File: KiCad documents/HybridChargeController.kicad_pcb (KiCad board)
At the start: 2 copper layers, 87 x 87 mm, 101 parts, among them P1 Load, P2 LI_balancer, P3 PV, P4 Extra, P5 LI, P6 LA, Q1 MMBT3904, Q10 MMBT3904, Q11 IPD90P04P4L-04, Q12 STL60P4LLF6, Q13 STL60P4LLF6, Q14 IPD90P04P4L-04, Q15 BSS138, Q16 BSS138, Q2 IPD90P04P4L-04, Q3 MMBT3904, Q4 IPD90P04P4L-04, Q5 IPD90P04P4L-04, Q6 MMBT3904, Q7 MMBT3904, Q8 MMBT3904, Q9 IPD90P04P4L-04, U1 LM358D, U2 bq76920, U3 cd4051, U4 LM358D, U5 LM358D

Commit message: ready for review
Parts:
- added G***: LOGO, MEI_logo:soldesign-logo, F.Cu at (164.9, 109.2)
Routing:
- net /GND: track 17.1 -> 60.8 mm, vias 4 -> 24
- net /COM+: track 178.3 -> 184.6 mm
- net /LOAD+: track 7.32 -> 13.6 mm
- net /LI+: track 32.7 -> 39.0 mm
- net Net-(F1-Pad2): track 20.0 -> 24.9 mm
- net Net-(R20-Pad1): track 6.08 -> 10.6 mm, vias 2 -> 0
- net Net-(F2-Pad2): track 22.1 -> 25.9 mm
- net /SDA3: track 11.9 -> 13.9 mm
- net Net-(R11-Pad1): track 8.50 -> 9.20 mm
- added copper zone on F.Cu, net /COM+
- added copper zone on B.Cu, net /GND
- added copper zone on F.Cu, net /GND
- added copper zone on F.Cu, net /LA+
- added copper zone on F.Cu, net /LA-
- added copper zone on F.Cu, net /LI-
- added copper zone on F.Cu, net /LOAD+
- added copper zone on F.Cu, net /LOAD-
- added copper zone on F.Cu, net /PV+
- added copper zone on F.Cu, net /PV-
- added copper zone on F.Cu, net Net-(D3-Pad2)
- added copper zone on F.Cu, net Net-(F1-Pad1)
- added copper zone on F.Cu, net Net-(F1-Pad2)
- added copper zone on F.Cu, net Net-(F2-Pad1)
- added copper zone on F.Cu, net Net-(F2-Pad2)
- added copper zone on F.Cu, net Net-(Q14-Pad3)
- added copper zone on F.Cu, net Net-(Q4-Pad3)
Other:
- board text added: "3.3V"
- board text added: "5V"
- board text added: "Alrt"
- board text added: "COM+"
- board text added: "Cell 1-2"
- board text added: "Cell 2-3"
- board text added: "Cell 3-4"
- board text added: "GND"
- board text added: "Hybrid Charge Controller"
- board text added: "LED"
- board text added: "MA"
- board text added: "MB"
- board text added: "MC"
- board text added: "MISO"
- board text added: "MO"
- board text added: "MOSI"
- board text added: "RST"
- board text added: "RX"
- board text added: "SCK"
- board text added: "SCL"
- board text added: "SDA"
- board text added: "SW LA"
- board text added: "SW LD"
- board text added: "SW PV"
- board text added: "TX"
- board text added: "made for Karana by"

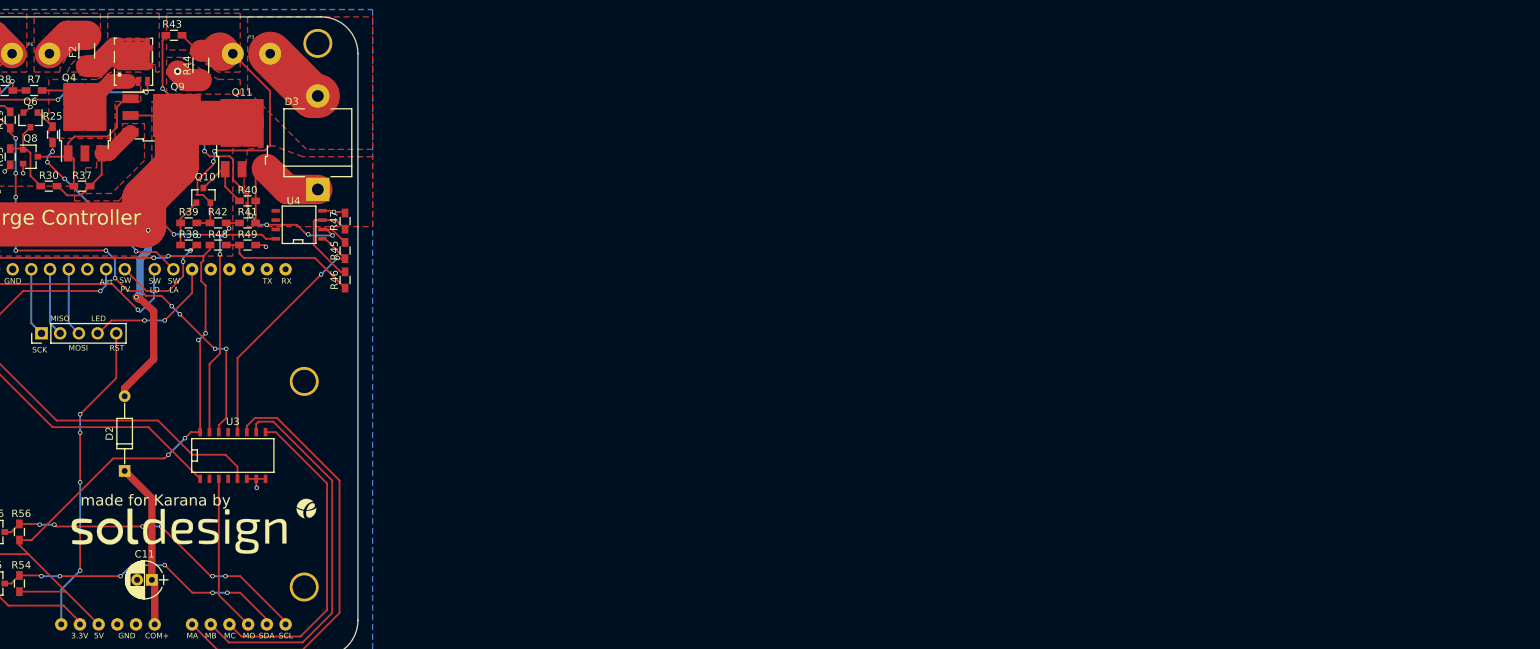
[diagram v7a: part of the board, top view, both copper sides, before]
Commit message: added a few comments for final check, played with the Silkscreen a bit
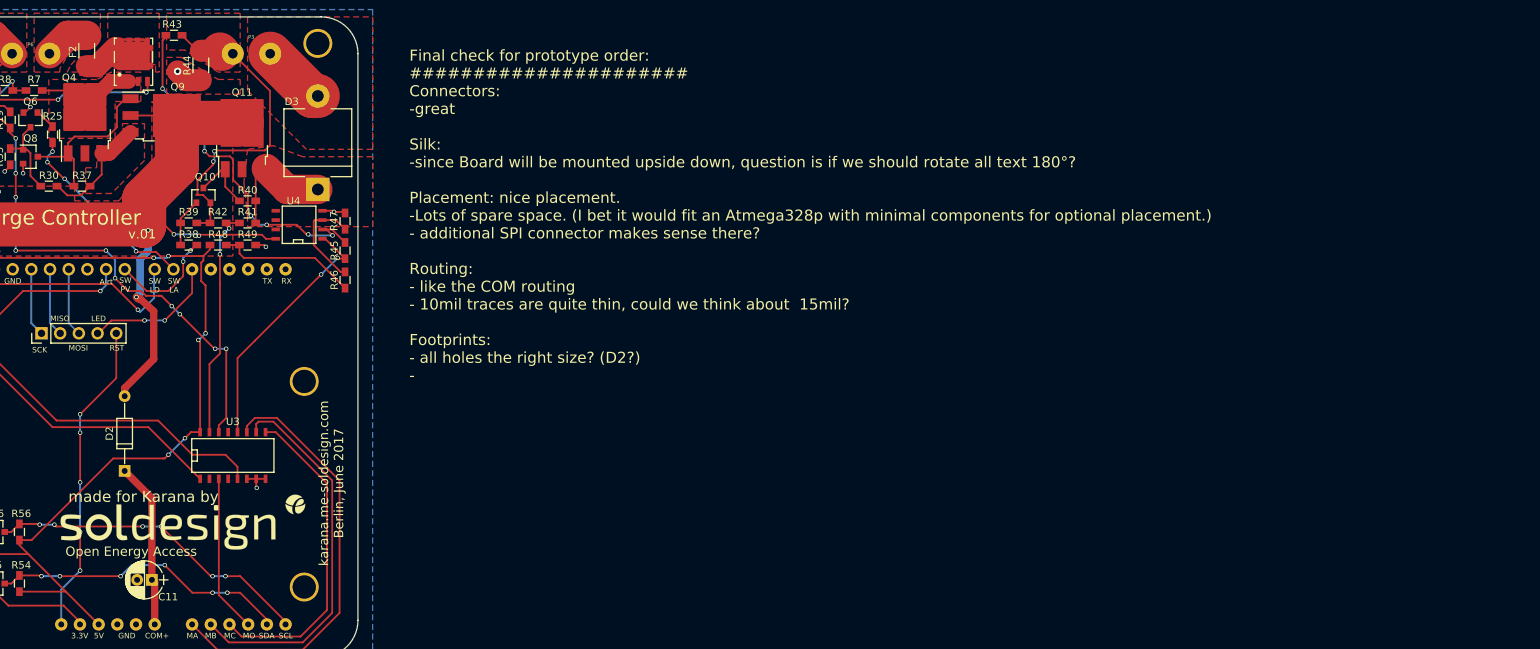
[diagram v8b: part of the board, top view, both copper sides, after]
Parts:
- moved G*** 1.60 mm to (163.4, 108.6)
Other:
- board text added: "Final check for prototype order: ###################### Connectors: -great Silk: -since Board will be mounted upside down, question is if we should rotate all text 180°? Placement: nice placement. -Lots of spare space. (I bet it would fit an Atmega328p with minimal components for optional placement.) - additional SPI connector makes sense there? Routing: - like the COM routing - 10mil traces are 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"
- board text added: "Open Energy Access"
- board text added: "karana.me-soldesign.com Berlin, June 2017"
- board text added: "v.01"
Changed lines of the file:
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@@
-(kicad_pcb (version 4) (host pcbnew 4.0.4-stable)
+(kicad_pcb (version 4) (host pcbnew 4.0.4+e1-6308~48~ubuntu15.10.1-stable)
   (general
     (links 248)
     (no_connects 2)
-    (area 99.924999 39.924999 187.075001 127.075001)
+    (area 97 39 189.000001 129.000001)
     (thickness 1.6)
-    (drawings 37)
+    (drawings 41)
     (tracks 866)
     (zones 0)
@@
     (0 F.Cu signal)
     (31 B.Cu signal hide)
-    (32 B.Adhes user)
-    (33 F.Adhes user)
+    (32 B.Adhes user hide)
+    (33 F.Adhes user hide)
     (34 B.Paste user)
     (35 F.Paste user)
@@
     (descr "CP, Radial series, Radial, pin pitch=2.00mm, , diameter=5mm, Electrolytic Capacitor")
     (tags "CP Radial series Radial pin pitch 2.00mm  diameter 5mm Electrolytic Capacitor")
-    (fp_text reference C11 (at 1 3.5 180) (layer F.SilkS)
+    (fp_text reference C11 (at -2.2138 -2.3212 180) (layer F.SilkS)
       (effects (font (size 1 1) (thickness 0.15)))
     )
@@
   )
   (module MEI_logo:soldesign-logo (layer F.Cu)
-    (at 164.9 109.2)
+    (at 163.3982 108.6358)
     (fp_text reference G*** (at 0 0) (layer F.SilkS) hide
       (effects (font (thickness 0.3)))
@@
       (xy 15.269597 -3.704432)) (layer F.SilkS) (width 0.01))
   )
-  (gr_text "Hybrid Charge Controller" (at 140.4 67.3) (layer F.SilkS)
-    (effects (font (size 2 2) (thickness 0.4)))
+  (gr_text "Final check for prototype order:\n######################\nConnectors: \n-great\n\nSilk: \n-since Board will be mounted upside down, question is if we should rotate all text 180°?\n\nPlacement: nice placement. \n-Lots of spare space. (I bet it would fit an Atmega328p with minimal components for optional placement.)\n- additional SPI connector makes sense there?\n\nRouting:\n- like the COM routing\n- 10mil traces are quite thin, could we think about  15mil?\n\nFootprints:\n- all holes the right size? (D2?)\n- \n\n" (at 193.9798 68.199) (layer F.SilkS)
+    (effects (font (size 1.5 1.5) (thickness 0.3)) (justify left))
+  )
+  (gr_text "karana.me-soldesign.com\nBerlin, June 2017" (at 183.388 103.378 90) (layer F.SilkS)
+    (effects (font (size 1.27 1.27) (thickness 0.2032)))
+  )
+  (gr_text v.01 (at 157.6832 69.5198) (layer F.SilkS)
+    (effects (font (size 1.27 1.27) (thickness 0.254)))
   )
-  (gr_text "made for Karana by" (at 159.5 105.7) (layer F.SilkS)
+  (gr_text "Open Energy Access" (at 156.1846 112.649) (layer F.SilkS)
+    (effects (font (size 1.27 1.27) (thickness 0.2032)))
+  )
+  (gr_text "made for Karana by" (at 157.861 105.2068) (layer F.SilkS)
     (effects (font (size 1.5 1.5) (thickness 0.25)))
   )
+  (gr_text "Hybrid Charge Controller" (at 140.4 67.3) (layer F.SilkS)
+    (effects (font (size 2 2) (thickness 0.4)))
+  )
   (gr_line (start 101.3 115) (end 103.5 115) (angle 90) (layer F.SilkS) (width 0.2))
